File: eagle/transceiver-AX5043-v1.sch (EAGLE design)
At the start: 33 parts, among them J1 2X8X1.27, J4 U.FL, J5 U.FL, J6 U.FL, U1 U-ONSEMI-AX5043, U2 LP2985XX-N, X1 TAITIEN-TY

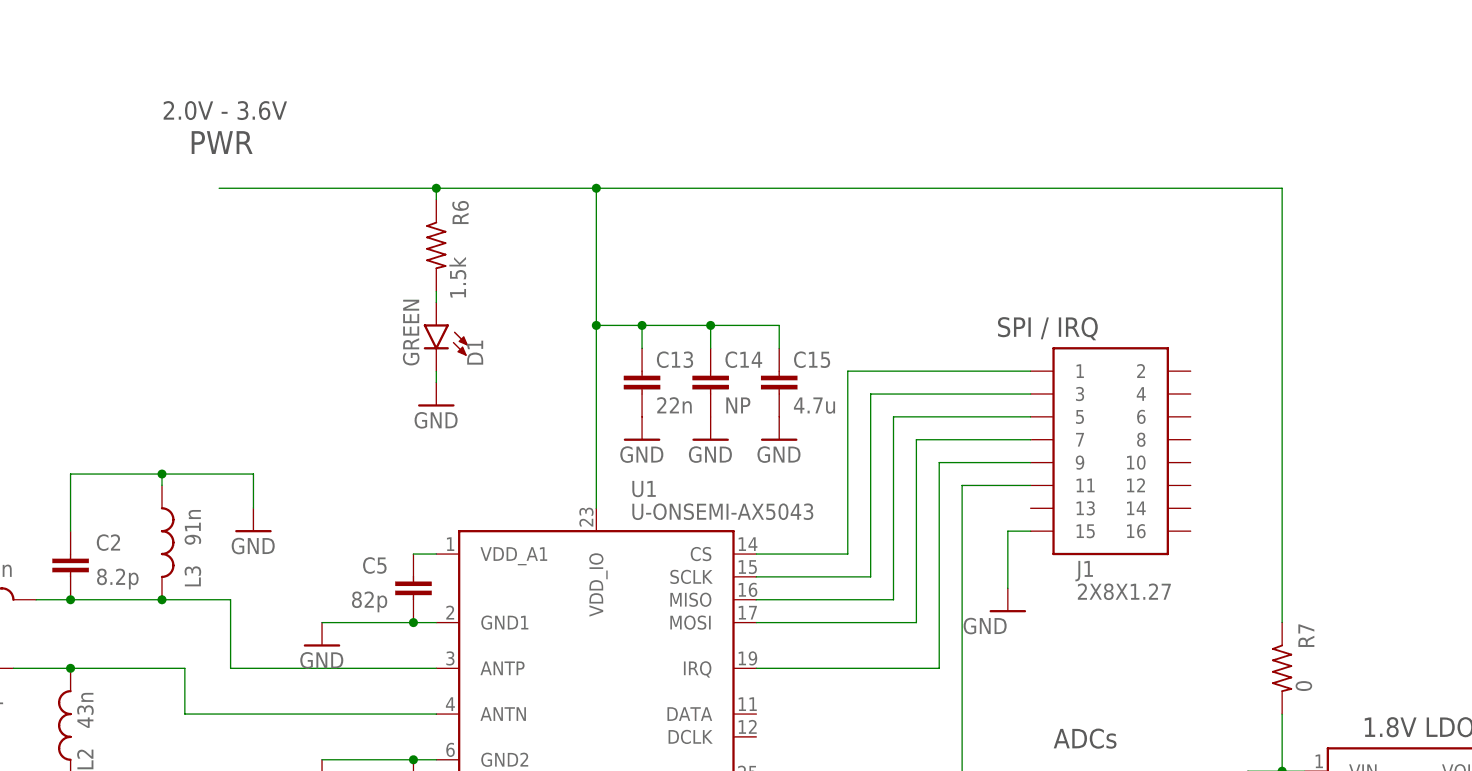
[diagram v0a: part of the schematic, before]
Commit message: Added the modified AX5043 transceiver block and some datasheets
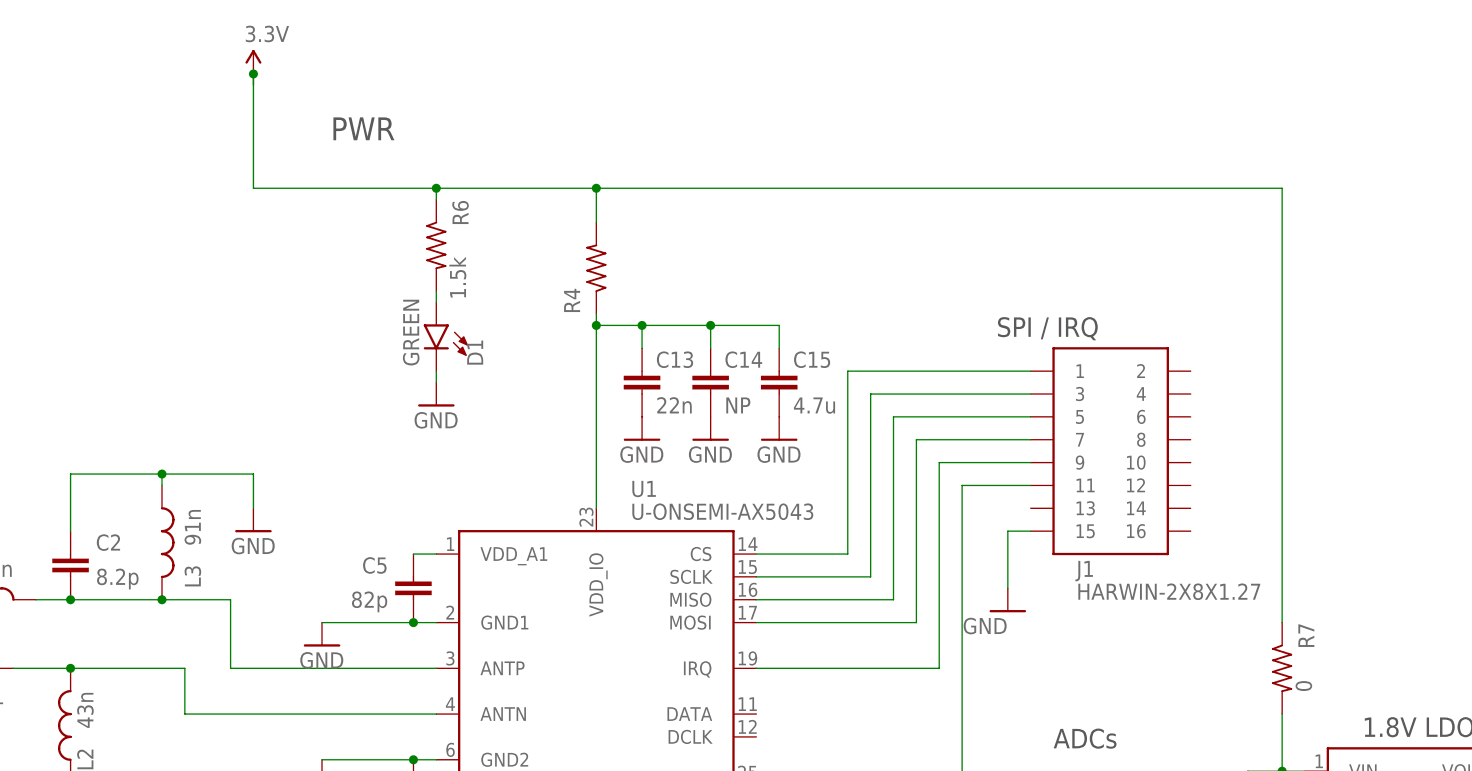
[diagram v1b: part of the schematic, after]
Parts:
- added R4: 0, oresat-rcl:R-US_0603-C-NOSILK
- J1: value 2X8X1.27 -> HARWIN-2X8X1.27; device J-2X8X1.27:2X8X1.27 -> J-Harwin-M50-3610842R-2X8X1.27_Male :HARWIN-2X8X1.27
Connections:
- removed net 2V7: C13.1, C14.1, C15.1, C17.1, R6.1, R7.1, R7.2, U1.VDD_IO, U2.EN, U2.VIN
- new net 3.3V: C13.1, C14.1, C15.1, C17.1, R4.1, R4.2, R6.1, R7.1, R7.2, U1.VDD_IO, U2.EN, U2.VIN
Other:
- note removed: "2.0V - 3.6V"
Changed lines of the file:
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@@
 <part name="J5" library="SparkFun-Connectors" deviceset="U.FL" device="" value="U.FL"/>
 <part name="J6" library="SparkFun-Connectors" deviceset="U.FL" device="" value="U.FL"/>
-<part name="J1" library="J-2X8X1.27" deviceset="2X8X1.27" device=""/>
+<part name="J1" library="J-Harwin-M50-3610842R-2X8X1.27_Male " deviceset="HARWIN-2X8X1.27" device=""/>
+<part name="P+1" library="SparkFun" deviceset="3.3V" device=""/>
+<part name="R4" library="oresat-rcl" deviceset="R-US_" device="0603-C-NOSILK" value="0"/>
 </parts>
 <sheets>
@@
 <text x="71.12" y="102.87" size="2.54" layer="97">Tx</text>
 <text x="59.69" y="77.47" size="2.54" layer="97">Ref-Out</text>
-<text x="104.14" y="184.15" size="2.54" layer="97" rot="MR0">PWR</text>
+<text x="119.888" y="185.674" size="2.54" layer="97" rot="MR0">PWR</text>
 <text x="186.69" y="163.83" size="2.159" layer="97">SPI / IRQ</text>
 <text x="193.04" y="97.79" size="2.159" layer="97">Control</text>
@@
 400 - 525 MHz
 800 - 1050 MHz</text>
-<text x="93.98" y="187.96" size="2.032" layer="97">2.0V - 3.6V</text>
 </plain>
 <instances>
@@
 <attribute name="NAME" x="195.58" y="137.16" size="1.778" layer="95" ratio="20"/>
 <attribute name="VALUE" x="195.58" y="134.62" size="1.778" layer="96" ratio="20"/>
+</instance>
+<instance part="P+1" gate="G$1" x="104.14" y="193.04" smashed="yes">
+<attribute name="VALUE" x="103.124" y="196.596" size="1.778" layer="96"/>
+</instance>
+<instance part="R4" gate="R" x="142.24" y="171.45" smashed="yes" rot="MR90">
+<attribute name="NAME" x="138.6586" y="166.37" size="1.778" layer="95" rot="MR90"/>
 </instance>
 </instances>
@@
 </segment>
 </net>
-<net name="SYSCLK" class="0">
+<net name="SYSCLK" class="1">
 <segment>
 <pinref part="U1" gate="G$1" pin="SYSCLK"/>
@@
 </segment>
 </net>
-<net name="ANTP" class="0">
+<net name="ANTP" class="1">
 <segment>
 <pinref part="C2" gate="CE" pin="2"/>
@@
 </segment>
 </net>
-<net name="ANTP1" class="0">
+<net name="ANTP1" class="1">
 <segment>
 <pinref part="C8" gate="CE" pin="2"/>
@@
 </segment>
 </net>
-<net name="2V7" class="0">
-<segment>
-<wire x1="142.24" y1="144.78" x2="142.24" y2="165.1" width="0.1524" layer="91"/>
-<pinref part="C15" gate="CE" pin="1"/>
-<wire x1="142.24" y1="165.1" x2="147.32" y2="165.1" width="0.1524" layer="91"/>
-<wire x1="147.32" y1="165.1" x2="154.94" y2="165.1" width="0.1524" layer="91"/>
-<wire x1="154.94" y1="165.1" x2="162.56" y2="165.1" width="0.1524" layer="91"/>
-<wire x1="162.56" y1="165.1" x2="162.56" y2="162.56" width="0.1524" layer="91"/>
-<pinref part="C14" gate="CE" pin="1"/>
-<wire x1="154.94" y1="162.56" x2="154.94" y2="165.1" width="0.1524" layer="91"/>
-<junction x="154.94" y="165.1"/>
-<pinref part="C13" gate="CE" pin="1"/>
-<wire x1="147.32" y1="162.56" x2="147.32" y2="165.1" width="0.1524" layer="91"/>
-<junction x="147.32" y="165.1"/>
-<pinref part="U1" gate="G$1" pin="VDD_IO"/>
-<junction x="142.24" y="165.1"/>
-<wire x1="142.24" y1="180.34" x2="142.24" y2="165.1" width="0.1524" layer="91"/>
-<wire x1="100.33" y1="180.34" x2="124.46" y2="180.34" width="0.1524" layer="91"/>
+<net name="LEDPWR" class="0">
+<segment>
+<pinref part="R6" gate="R" pin="2"/>
+<pinref part="D1" gate="G$1" pin="A"/>
+<wire x1="124.46" y1="168.91" x2="124.46" y2="167.64" width="0.1524" layer="91"/>
+</segment>
+</net>
+<net name="N$1" class="0">
+<segment>
+<pinref part="C5" gate="CE" pin="1"/>
+<pinref part="U1" gate="G$1" pin="VDD_A1"/>
+<wire x1="121.92" y1="139.7" x2="124.46" y2="139.7" width="0.1524" layer="91"/>
+</segment>
+</net>
+<net name="N$30" class="0">
+<segment>
+<pinref part="C6" gate="CE" pin="2"/>
+<pinref part="U1" gate="G$1" pin="VDD_A2"/>
+<wire x1="121.92" y1="109.22" x2="124.46" y2="109.22" width="0.1524" layer="91"/>
+</segment>
+</net>
+<net name="N$27" class="0">
+<segment>
+<pinref part="U2" gate="G$1" pin="BYPASS"/>
+<pinref part="C16" gate="CE" pin="1"/>
+<wire x1="246.38" y1="107.95" x2="254" y2="107.95" width="0.1524" layer="91"/>
+</segment>
+</net>
+<net name="N$20" class="2">
+<segment>
+<pinref part="C7" gate="CE" pin="2"/>
+<pinref part="L1" gate="L" pin="1"/>
+<wire x1="62.23" y1="130.81" x2="67.31" y2="130.81" width="0.1524" layer="91"/>
+<wire x1="67.31" y1="130.81" x2="67.31" y2="134.62" width="0.1524" layer="91"/>
+<pinref part="C1" gate="CE" pin="1"/>
+<wire x1="69.85" y1="127" x2="67.31" y2="127" width="0.1524" layer="91"/>
+<wire x1="67.31" y1="127" x2="67.31" y2="130.81" width="0.1524" layer="91"/>
+<junction x="67.31" y="130.81"/>
+</segment>
+</net>
+<net name="N$6" class="2">
+<segment>
+<pinref part="C4" gate="CE" pin="2"/>
+<pinref part="X1" gate="G$1" pin="OUT"/>
+<wire x1="175.26" y1="80.01" x2="175.26" y2="72.39" width="0.1524" layer="91"/>
+<wire x1="175.26" y1="72.39" x2="187.96" y2="72.39" width="0.1524" layer="91"/>
+</segment>
+</net>
+<net name="PWRAMP" class="0">
+<segment>
+<pinref part="U1" gate="G$1" pin="PWRAMP"/>
+<wire x1="160.02" y1="101.6" x2="182.88" y2="101.6" width="0.1524" layer="91"/>
+<wire x1="182.88" y1="101.6" x2="182.88" y2="147.32" width="0.1524" layer="91"/>
+<pinref part="J1" gate="G$1" pin="11"/>
+<wire x1="182.88" y1="147.32" x2="190.5" y2="147.32" width="0.1524" layer="91"/>
+</segment>
+</net>
+<net name="3.3V" class="0">
+<segment>
+<pinref part="P+1" gate="G$1" pin="3.3V"/>
+<wire x1="104.14" y1="193.04" x2="104.14" y2="191.77" width="0.1524" layer="91"/>
 <pinref part="R6" gate="R" pin="1"/>
+<wire x1="104.14" y1="180.34" x2="124.46" y2="180.34" width="0.1524" layer="91"/>
 <wire x1="124.46" y1="180.34" x2="142.24" y2="180.34" width="0.1524" layer="91"/>
 <wire x1="124.46" y1="179.07" x2="124.46" y2="180.34" width="0.1524" layer="91"/>
@@
 <wire x1="218.44" y1="180.34" x2="218.44" y2="132.08" width="0.1524" layer="91"/>
 <junction x="142.24" y="180.34"/>
+<wire x1="104.14" y1="181.61" x2="104.14" y2="180.34" width="0.1524" layer="91"/>
+<wire x1="142.24" y1="180.34" x2="142.24" y2="176.53" width="0.1524" layer="91"/>
+<pinref part="R4" gate="R" pin="2"/>
+<wire x1="104.14" y1="193.04" x2="104.14" y2="181.61" width="0.1524" layer="91"/>
+<junction x="104.14" y="193.04"/>
 </segment>
 <segment>
@@
 <wire x1="214.63" y1="115.57" x2="218.44" y2="115.57" width="0.1524" layer="91"/>
 </segment>
-</net>
-<net name="LEDPWR" class="0">
-<segment>
-<pinref part="R6" gate="R" pin="2"/>
-<pinref part="D1" gate="G$1" pin="A"/>
-<wire x1="124.46" y1="168.91" x2="124.46" y2="167.64" width="0.1524" layer="91"/>
-</segment>
-</net>
-<net name="N$1" class="0">
-<segment>
-<pinref part="C5" gate="CE" pin="1"/>
-<pinref part="U1" gate="G$1" pin="VDD_A1"/>
-<wire x1="121.92" y1="139.7" x2="124.46" y2="139.7" width="0.1524" layer="91"/>
-</segment>
-</net>
-<net name="N$30" class="0">
-<segment>
-<pinref part="C6" gate="CE" pin="2"/>
-<pinref part="U1" gate="G$1" pin="VDD_A2"/>
-<wire x1="121.92" y1="109.22" x2="124.46" y2="109.22" width="0.1524" layer="91"/>
-</segment>
-</net>
-<net name="N$27" class="0">
-<segment>
-<pinref part="U2" gate="G$1" pin="BYPASS"/>
-<pinref part="C16" gate="CE" pin="1"/>
-<wire x1="246.38" y1="107.95" x2="254" y2="107.95" width="0.1524" layer="91"/>
-</segment>
-</net>
-<net name="N$20" class="2">
-<segment>
-<pinref part="C7" gate="CE" pin="2"/>
-<pinref part="L1" gate="L" pin="1"/>
-<wire x1="62.23" y1="130.81" x2="67.31" y2="130.81" width="0.1524" layer="91"/>
-<wire x1="67.31" y1="130.81" x2="67.31" y2="134.62" width="0.1524" layer="91"/>
-<pinref part="C1" gate="CE" pin="1"/>
-<wire x1="69.85" y1="127" x2="67.31" y2="127" width="0.1524" layer="91"/>
-<wire x1="67.31" y1="127" x2="67.31" y2="130.81" width="0.1524" layer="91"/>
-<junction x="67.31" y="130.81"/>
-</segment>
-</net>
-<net name="N$6" class="2">
-<segment>
-<pinref part="C4" gate="CE" pin="2"/>
-<pinref part="X1" gate="G$1" pin="OUT"/>
-<wire x1="175.26" y1="80.01" x2="175.26" y2="72.39" width="0.1524" layer="91"/>
-<wire x1="175.26" y1="72.39" x2="187.96" y2="72.39" width="0.1524" layer="91"/>
-</segment>
-</net>
-<net name="PWRAMP" class="0">
-<segment>
-<pinref part="U1" gate="G$1" pin="PWRAMP"/>
-<wire x1="160.02" y1="101.6" x2="182.88" y2="101.6" width="0.1524" layer="91"/>
-<wire x1="182.88" y1="101.6" x2="182.88" y2="147.32" width="0.1524" layer="91"/>
-<pinref part="J1" gate="G$1" pin="11"/>
-<wire x1="182.88" y1="147.32" x2="190.5" y2="147.32" width="0.1524" layer="91"/>
-</segment>
-</net>
+<segment>
+<pinref part="C15" gate="CE" pin="1"/>
+<wire x1="162.56" y1="165.1" x2="162.56" y2="162.56" width="0.1524" layer="91"/>
+<wire x1="154.94" y1="165.1" x2="162.56" y2="165.1" width="0.1524" layer="91"/>
+<pinref part="C14" gate="CE" pin="1"/>
+<wire x1="154.94" y1="162.56" x2="154.94" y2="165.1" width="0.1524" layer="91"/>
+<junction x="154.94" y="165.1"/>
+<wire x1="147.32" y1="165.1" x2="154.94" y2="165.1" width="0.1524" layer="91"/>
+<pinref part="C13" gate="CE" pin="1"/>
+<wire x1="147.32" y1="162.56" x2="147.32" y2="165.1" width="0.1524" layer="91"/>
+<junction x="147.32" y="165.1"/>
+<wire x1="142.24" y1="165.1" x2="147.32" y2="165.1" width="0.1524" layer="91"/>
+<junction x="142.24" y="165.1"/>
+<wire x1="142.24" y1="166.37" x2="142.24" y2="165.1" width="0.1524" layer="91"/>
+<wire x1="142.24" y1="144.78" x2="142.24" y2="165.1" width="0.1524" layer="91"/>
+<pinref part="U1" gate="G$1" pin="VDD_IO"/>
+<pinref part="R4" gate="R" pin="1"/>
+</segment>
+</net>
